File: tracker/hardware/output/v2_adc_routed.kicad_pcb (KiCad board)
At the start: 2 copper layers, 50 x 40 mm, 17 parts, among them U1 ESP32-C3, U2 LR2021F33, U3 MAX-M10S, U4 TPS7A02

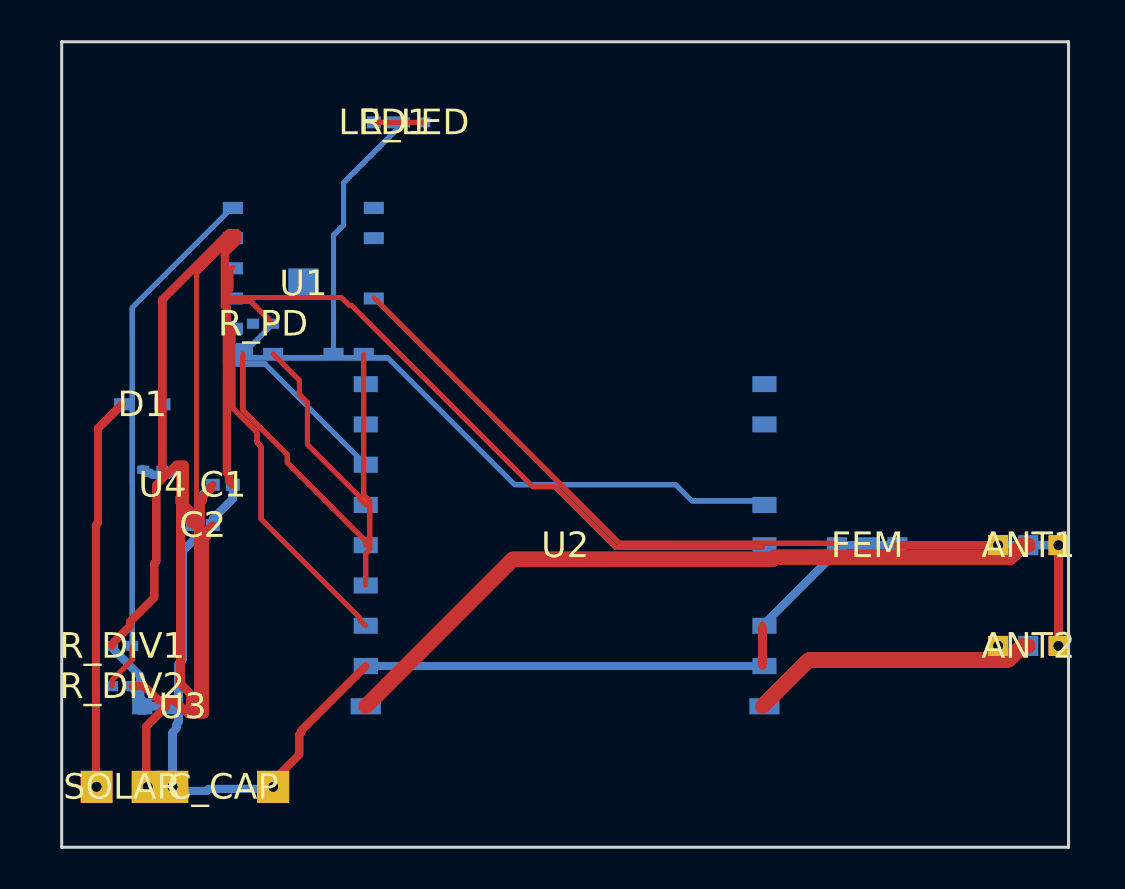
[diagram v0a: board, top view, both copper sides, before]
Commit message: fix: ESP32-C3 GPIO5/GPIO6 pad collision — shift bottom row inboard by one pitch
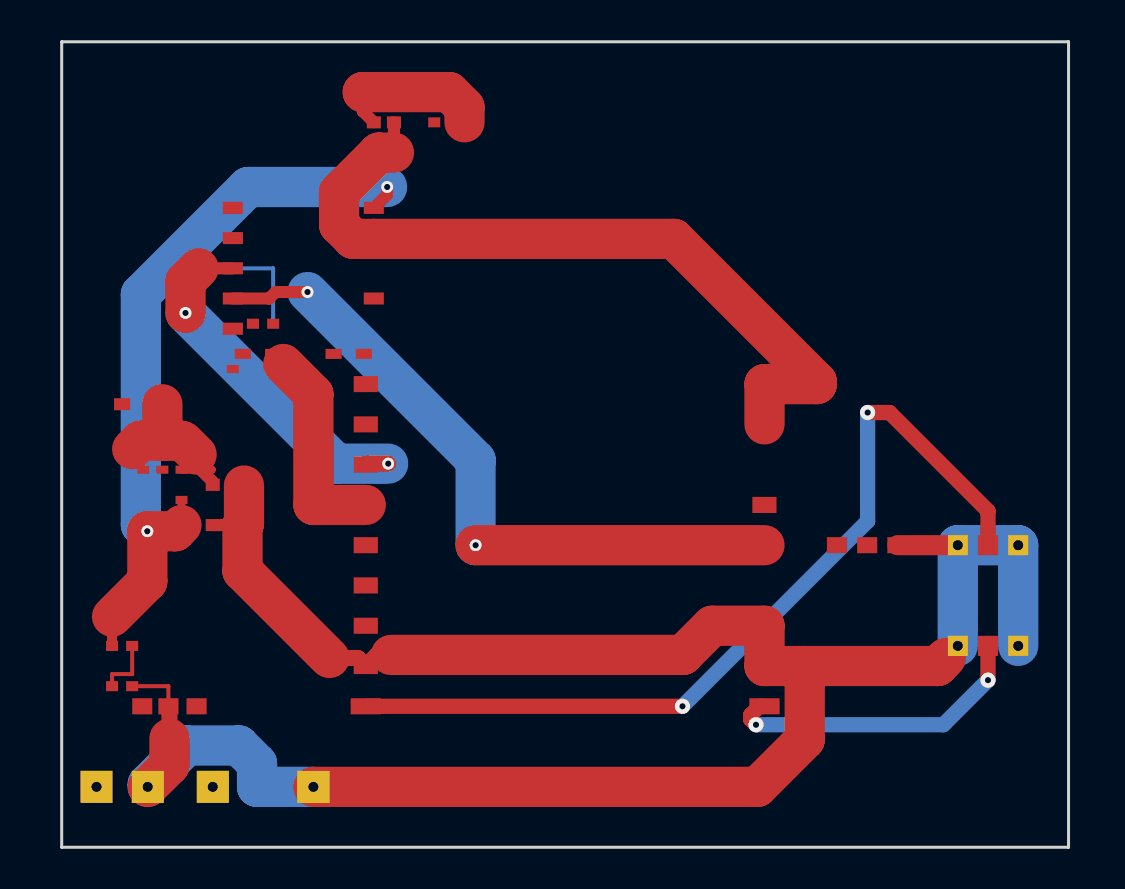
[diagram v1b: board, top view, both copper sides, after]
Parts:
- moved ANT1 2.00 mm to (46.0, 25.0)
- moved ANT2 2.00 mm to (46.0, 30.0)
- moved C_CAP 2.00 mm to (10.0, 37.0)
- moved R_LED 1.50 mm to (19.0, 4.00)
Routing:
- net SPI_SCK: track 33.1 -> 0.00 mm
- net VCAP: track 42.1 -> 10.3 mm
- net LR2021_DIO9: track 29.3 -> 0.00 mm
- net FEM_TX: track 28.1 -> 0.00 mm
- net GND: track 121.6 -> 148.4 mm
- net GPS_RX: track 24.0 -> 0.00 mm
- net VDIV_MID: track 26.3 -> 3.00 mm
- net SOLAR_IN: track 19.5 -> 0.00 mm
- net 3V3: track 19.1 -> 37.9 mm, vias 0 -> 2
- net LR2021_BUSY: track 17.5 -> 0.00 mm
- net RF_2G4_2400: track 0.00 -> 15.6 mm, vias 0 -> 2
- net STATUS_LED: track 12.9 -> 0.00 mm
- net SPI_MOSI: track 0.00 -> 10.9 mm
- net RF_SUB_868: track 36.2 -> 43.8 mm, vias 0 -> 2
- net SPI_MISO: track 16.6 -> 23.2 mm, vias 0 -> 2
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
